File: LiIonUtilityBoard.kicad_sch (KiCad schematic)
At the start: 42 parts, among them J1 USB4510-03-1-A, J2 Conn_02x07_Odd_Even, Q1 PMDPB30XN, U1 MAX77757JEFG420+, U2 bq298215, U3 MAX17260SETD, U4 ISL91127IR

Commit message: Sync project status
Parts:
- removed J1: USB4510-03-1-A, LUBParts:GCT_USB4510-03-1-A_REVA, symbol LUBParts:USB4510-03-1-A
- added J1: USBC_Swapped, Connector_USB:USB_C_Receptacle_GCT_USB4085, symbol LUBParts:USBC_Swapped
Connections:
- net GND: now also J1.A1 (GND), J1.A12 (GND), J1.B1 (GND), J1.B12 (GND), J1.S1 (SHIELD)
- net at C1.2, U1.23_24 (CHGIN): now also J1.A4 (VBUS), J1.A9 (VBUS), J1.B4 (VBUS), J1.B9 (VBUS)
- net at U1.4 (CC2): now also J1.B5 (CC2)
- net at U1.5 (CC1): now also J1.A5 (CC1)
- net at U1.6 (DP): now also J1.A6 (D+), J1.B6 (D+)
- net at U1.7 (DN): now also J1.A7 (D-), J1.B7 (D-)
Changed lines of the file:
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@@
     (pin "2")
-  )
-  (symbol (lib_id "LUBParts:USB4510-03-1-A") (at 30.48 58.42 0) (unit 1)
-    (in_bom yes) (on_board yes) (fields_autoplaced)
-    (property "Reference" "J1" (id 0) (at 30.48 35.56 0))
-    (property "Value" "USB4510-03-1-A" (id 1) (at 30.48 38.1 0))
-    (property "Footprint" "LUBParts:GCT_USB4510-03-1-A_REVA" (id 2) (at 33.02 33.02 0)
-      (effects (font (size 1.27 1.27)) hide)
-    )
-    (property "Datasheet" "https://www.mouser.com/datasheet/2/837/usb4510-2583684.pdf" (id 3) (at 33.02 35.56 0)
-      (effects (font (size 1.27 1.27)) hide)
-    )
-    (pin "S2")
-    (pin "S3")
-    (pin "S4")
-    (pin "A1_B12")
-    (pin "A4_B9")
-    (pin "A5")
-    (pin "A6")
-    (pin "A7")
-    (pin "A8")
-    (pin "B1_A12")
-    (pin "B4_A9")
-    (pin "B5")
-    (pin "B6")
-    (pin "B7")
-    (pin "B8")
-    (pin "S1")
   )
   (symbol (lib_id "power:+BATT") (at 142.24 30.48 0) (unit 1)
@@
     )
     (pin "1")
+  )
+  (symbol (lib_id "LUBParts:USBC_Swapped") (at 30.48 58.42 0) (unit 1)
+    (in_bom yes) (on_board yes) (fields_autoplaced)
+    (property "Reference" "J1" (id 0) (at 30.48 35.56 0))
+    (property "Value" "USBC_Swapped" (id 1) (at 30.48 38.1 0))
+    (property "Footprint" "Connector_USB:USB_C_Receptacle_GCT_USB4085" (id 2) (at 34.29 58.42 0)
+      (effects (font (size 1.27 1.27)) hide)
+    )
+    (property "Datasheet" "https://www.usb.org/sites/default/files/documents/usb_type-c.zip" (id 3) (at 33.02 33.02 0)
+      (effects (font (size 1.27 1.27)) hide)
+    )
+    (pin "A1")
+    (pin "A12")
+    (pin "A4")
+    (pin "A5")
+    (pin "A6")
+    (pin "A7")
+    (pin "A8")
+    (pin "A9")
+    (pin "B1")
+    (pin "B12")
+    (pin "B4")
+    (pin "B5")
+    (pin "B6")
+    (pin "B7")
+    (pin "B8")
+    (pin "B9")
+    (pin "S1")
   )
   (symbol (lib_id "HABParts:+SYS") (at 222.25 116.84 0) (unit 1)
@@
       (reference "D2") (unit 1) (value "STAT") (footprint "LED_SMD:LED_0603_1608Metric")
     )
-    (path "/4e49e0e8-6abb-46ed-98fe-4917dffc1239"
-      (reference "J1") (unit 1) (value "USB4510-03-1-A") (footprint "LUBParts:GCT_USB4510-03-1-A_REVA")
+    (path "/b74f0465-f2ea-4056-83de-03fca2fdcca4"
+      (reference "J1") (unit 1) (value "USBC_Swapped") (footprint "Connector_USB:USB_C_Receptacle_GCT_USB4085")
     )
     (path "/f661236d-0f2a-4659-9c88-b91865309fb5"

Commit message: Finalize Schematic
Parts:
- removed C11: 10u, Capacitor_SMD:C_0805_2012Metric, symbol Device:C_Small
- removed C13, C14: 22u, Capacitor_SMD:C_0805_2012Metric, symbol Device:C_Small
- removed C15: 0.47u, Capacitor_SMD:C_0402_1005Metric, symbol Device:C_Small
- removed C6: 0.1u, Capacitor_SMD:C_0402_1005Metric, symbol Device:C_Small
- removed J2: Conn_02x07_Odd_Even, Connector_PinHeader_2.54mm:PinHeader_2x07_P2.54mm_Vertical, symbol Connector_Generic:Conn_02x07_Odd_Even
- removed L2: 1u, Inductor_SMD:L_Taiyo-Yuden_NR-60xx, symbol Device:L_Small
- removed R12: 10m, Resistor_SMD:R_0612_1632Metric, symbol Device:R_Small
- removed R13, R4: 10K, Resistor_SMD:R_0402_1005Metric, symbol Device:R_Small
- removed U2: bq298215, LUBParts:BQ298009RUGR, symbol HABParts:bq298215
- removed U3: MAX17260SETD, Package_DFN_QFN:TDFN-14-1EP_3x3mm_P0.4mm_EP1.78x2.35mm, symbol HABParts:MAX17260SETD
- removed U4: ISL91127IR, Package_DFN_QFN:QFN-20-1EP_4x4mm_P0.5mm_EP2.7x2.7mm_ThermalVias, symbol HABParts:ISL91127IR
- added C11: 47u, symbol Device:C_Polarized_Small
- added J2: Output, symbol Connector:Screw_Terminal_01x03
- added JP1: IFAST1, Jumper:SolderJumper-2_P1.3mm_Bridged_Pad1.0x1.5mm, symbol Jumper:Jumper_2_Bridged
- added JP2: IFAST2, Jumper:SolderJumper-2_P1.3mm_Bridged_Pad1.0x1.5mm, symbol Jumper:Jumper_2_Bridged
- added R8: 7.32K, symbol Device:R_Small
- added R9: 8.66K, symbol Device:R_Small
- added U2: bq298019, LUBParts:BQ298009RUGR, symbol LUBParts:bq298019
- BT1: footprint Connector_PinHeader_2.54mm:PinHeader_1x02_P2.54mm_Vertical -> (none)
- C1, C2, C3: footprint Capacitor_SMD:C_0603_1608Metric -> (none)
- C10: renamed from C12; footprint Capacitor_SMD:C_0805_2012Metric -> (none)
- C4: renamed from C7; footprint Capacitor_SMD:C_0805_2012Metric -> (none)
- C5: renamed from C8; footprint Capacitor_SMD:C_0805_2012Metric -> (none)
- C6: renamed from C9; footprint Capacitor_SMD:C_0805_2012Metric -> (none)
- C7: renamed from C10; footprint Capacitor_SMD:C_0805_2012Metric -> (none)
- C8: renamed from C5; footprint Capacitor_SMD:C_0402_1005Metric -> (none)
- C9: renamed from C4; footprint Capacitor_SMD:C_0402_1005Metric -> (none)
- JP3: renamed from JP1; value Jumper_3_Bridged12 -> THM_EN
- L1: value 1u -> 0.47u; footprint Inductor_SMD:L_Taiyo-Yuden_NR-60xx -> (none)
- Q1: footprint LUBParts:DMN1025UFDB7 -> LUBParts:SON65P200X200X65-8N
- R1, R2, R3: footprint Resistor_SMD:R_0402_1005Metric -> (none)
- R10: renamed from R9; value 2.26m -> 9.0m; footprint Resistor_SMD:R_2512_6332Metric -> (none)
- R11: renamed from R10; footprint Resistor_SMD:R_0402_1005Metric -> (none)
- R12: renamed from R11; footprint Resistor_SMD:R_0402_1005Metric -> (none)
- R4: renamed from R5; footprint Resistor_SMD:R_0603_1608Metric -> (none)
- R5: renamed from R6; footprint Resistor_SMD:R_0603_1608Metric -> (none)
- R6: renamed from R7; footprint Resistor_SMD:R_0603_1608Metric -> (none)
- R7: renamed from R8; value 18.2K -> 6.65K; footprint Resistor_SMD:R_0402_1005Metric -> (none)
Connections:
- net +BATT: now also Q1.1 (S1), R6.2
- net +SYS: now also C11.1, J2.1 (Pin_1)
- net ENBST: now also J2.3 (Pin_3)
- net GND: now also C11.2, J2.2 (Pin_2), JP2.1 (A), R9.1, U2.4 (CS), U2.5 (CTR); no longer R7.1
- net at C8.1, R11.1: now also U2.2 (VDD)
- net at BT1.2 (-), C8.2, R10.1: now also U2.3 (VSS)
- net IFAST: now reaches R7.2, U1.12 (IFAST)
- net at Q1.5 (G2): now also U2.8 (CSG)
- net at Q1.2 (G1): now also U2.7 (DSG)
- net at R12.1: now also U2.1 (BAT)
- net at R6.1: now also U2.6 (PACK)
- new net: JP1.2 (B), R7.1, R8.2
- new net: JP1.1 (A), JP2.2 (B), R8.1, R9.2
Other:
- moved on the sheet: BT1, C1, C10, C2, C3, C4, C5, C6, C7, C8, C9, D1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

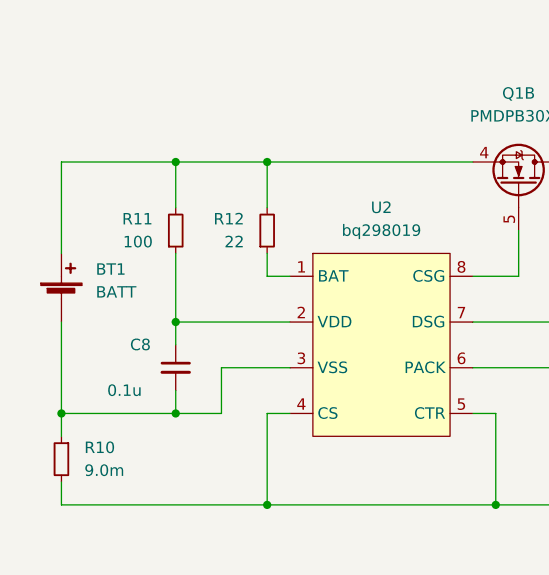
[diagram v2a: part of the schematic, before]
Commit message: Finshed schematic and associated footprints
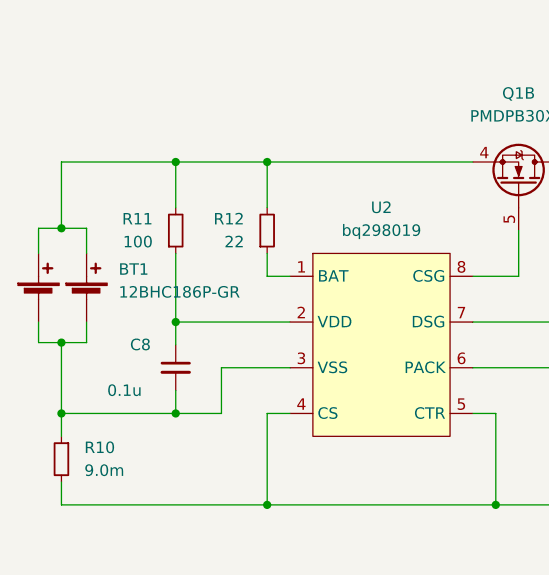
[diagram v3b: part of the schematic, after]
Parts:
- removed BT1: BATT, symbol Device:Battery_Cell
- added BT1: 12BHC186P-GR, LUBParts:12BHC186P-GR, symbol LUBParts:12BHC186P-GR
- C1, C2, C3, C8, C9: footprint (none) -> Capacitor_SMD:C_0402_1005Metric
- C10: footprint (none) -> Capacitor_SMD:C_0805_2012Metric
- C11: footprint (none) -> Capacitor_SMD:CP_Elec_5x5.3
- C4, C5, C6, C7: footprint (none) -> Capacitor_SMD:C_0603_1608Metric
- J2: footprint (none) -> LUBParts:CUI_TB002-500-03BE
- L1: footprint (none) -> Inductor_SMD:L_1008_2520Metric
- R1, R11, R12, R2, R3, R4, R5, R6, R7, R8, R9: footprint (none) -> Resistor_SMD:R_0402_1005Metric
- R10: footprint (none) -> Resistor_SMD:R_0603_1608Metric
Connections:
- net at C8.2, R10.1, U2.3 (VSS): now also BT1.2 (1-), BT1.4 (2-)
- net at Q1.4 (S2), R11.2, R12.2: now also BT1.1 (1+), BT1.3 (2+)

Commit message: Finish Routing
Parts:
- JP3: footprint Jumper:SolderJumper-3_P1.3mm_Open_Pad1.0x1.5mm_NumberLabels -> Jumper:SolderJumper-3_P1.3mm_Bridged12_Pad1.0x1.5mm_NumberLabels
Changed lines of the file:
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@@
     (property "Reference" "JP3" (id 0) (at 140.97 95.25 0))
     (property "Value" "THM_EN" (id 1) (at 149.86 95.25 0))
-    (property "Footprint" "Jumper:SolderJumper-3_P1.3mm_Open_Pad1.0x1.5mm_NumberLabels" (id 2) (at 144.78 99.06 0)
+    (property "Footprint" "Jumper:SolderJumper-3_P1.3mm_Bridged12_Pad1.0x1.5mm_NumberLabels" (id 2) (at 144.78 99.06 0)
       (effects (font (size 1.27 1.27)) hide)
     )
@@
     )
     (path "/b1ff7a83-c491-4ffd-a190-8e165d0ec59a"
-      (reference "JP3") (unit 1) (value "THM_EN") (footprint "Jumper:SolderJumper-3_P1.3mm_Open_Pad1.0x1.5mm_NumberLabels")
+      (reference "JP3") (unit 1) (value "THM_EN") (footprint "Jumper:SolderJumper-3_P1.3mm_Bridged12_Pad1.0x1.5mm_NumberLabels")
     )
     (path "/c43d852e-e4e8-4c44-a6f4-06886a37d483"
